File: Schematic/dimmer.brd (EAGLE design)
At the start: 51 x 51 mm, 18 parts, among them Q1 IRF840, T1 BC547

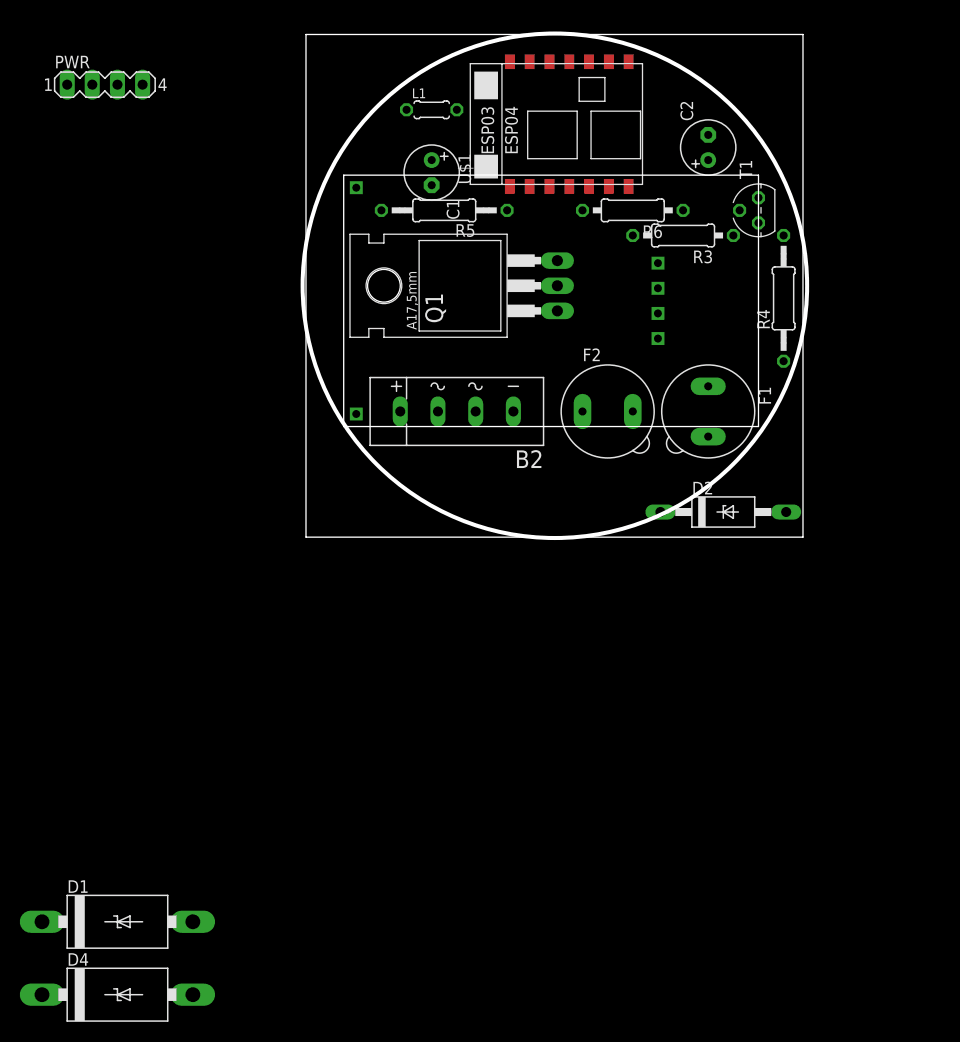
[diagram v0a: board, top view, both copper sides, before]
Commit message: Add tasters
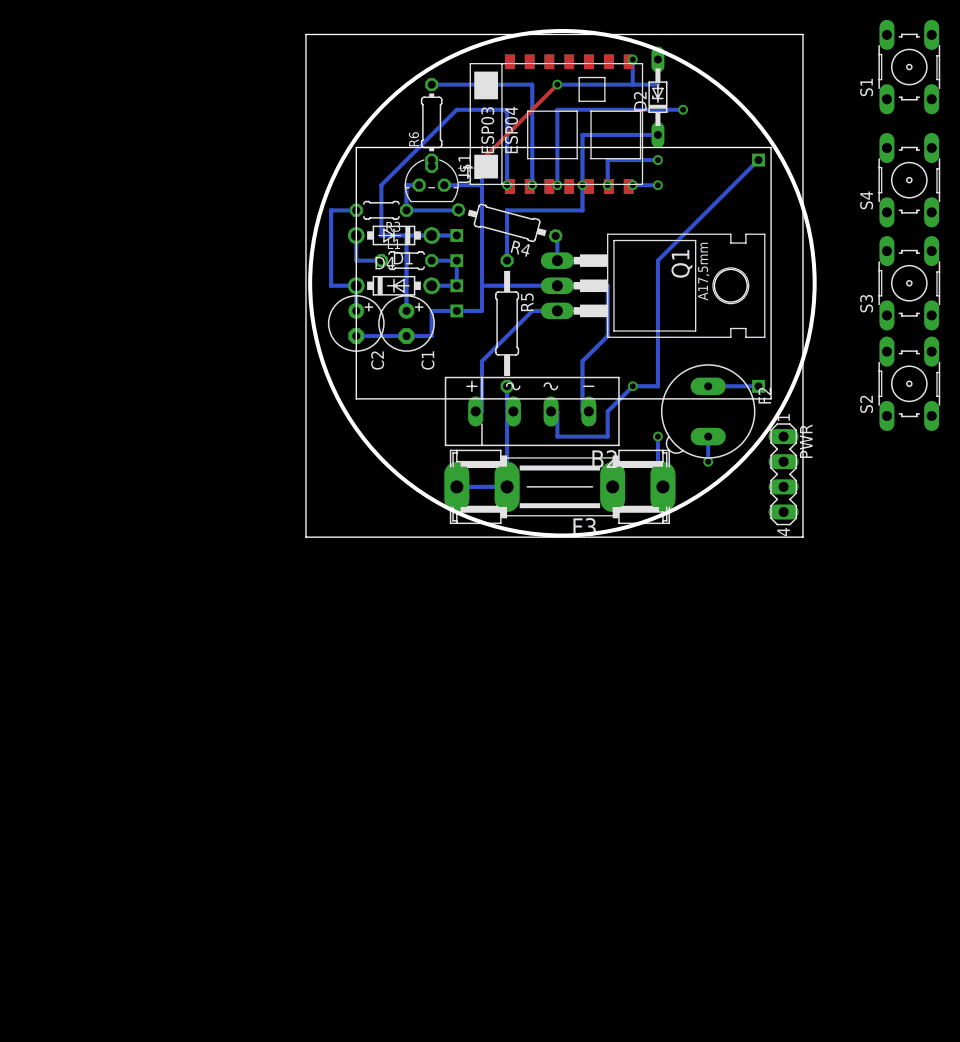
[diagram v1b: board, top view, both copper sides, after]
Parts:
- removed F1: 1A flink, fuse:19560
- added F3: 1A flink, fuse:SHK20L
- added S1, S2, S3, S4: (no value), switch-omron:B3F-10XX
- D1, D4: value 1N5819 -> 1N5817-B; device diode:C4111-15 -> diode:DO41-7.6
- D2: device diode:F126Z12 -> diode:DO34Z7
- R3: device rcl:0207/10 -> rcl:0204/5
- R4: device rcl:0207/12 -> rcl:0207/10
- R6: device rcl:0207/10 -> rcl:0204/7
- moved PWR 79.1 mm to (48.3, 6.35), turned to 270 degrees
- moved D4 76.9 mm to (8.89, 25.4)
- moved D1 74.8 mm to (8.89, 30.5), turned to 180 degrees
- moved U$2 45.8 mm to (48.3, 12.7), flipped to the top
- moved D2 42.4 mm to (35.6, 44.5), turned to 90 degrees
- moved C2 39.8 mm to (5.08, 21.6), turned to 270 degrees
- moved T1 33.1 mm to (12.7, 35.6), turned to 0 degrees
- moved R3 30.6 mm to (7.62, 33.0)
- moved R4 29.0 mm to (20.3, 31.8), turned to 165 degrees
- moved R6 22.2 mm to (12.7, 41.9), turned to 90 degrees
- moved C1 15.5 mm to (10.2, 21.6)
- moved L1 15.5 mm to (10.2, 27.9)
- moved R5 13.1 mm to (20.3, 21.6), turned to 270 degrees
- moved Q1 12.7 mm to (31.8, 25.4), turned to 270 degrees
- moved F2 10.2 mm to (40.6, 12.7), turned to 270 degrees
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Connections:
- new net N$13: S2.1, S2.2, U$1.GPIO0
- new net N$14: S3.1, S3.2, U$1.GPIO2
- new net N$15: S1.1, S1.2, U$1.GPIO18
- new net N$16: S4.1, S4.2, U$1.GPIO12
- net GND: now also S1.3, S1.4, S2.3, S2.4, S3.3, S3.4, S4.3, S4.4
- net N$17: now also B2.AC2, F3.2A; no longer B2.AC1, F1.2
- net N$31: now also F3.1A; no longer F1.1
- net N$4: now also B2.AC1; no longer B2.AC2
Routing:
- net GND: track 0.00 -> 88.0 mm, vias 0 -> 3
- net +3V3: track 0.00 -> 44.3 mm, vias 0 -> 1
- net N$4: track 0.00 -> 44.2 mm, vias 0 -> 1
- net N$7: track 0.00 -> 28.7 mm, vias 0 -> 1
- net N$16: track 0.00 -> 21.4 mm, vias 0 -> 2
- net N$12: track 0.00 -> 20.7 mm, vias 0 -> 1
- net N$17: track 0.00 -> 15.9 mm
- net N$21: track 0.00 -> 15.4 mm
- net +5V: track 0.00 -> 15.2 mm
- net N$2: track 0.00 -> 9.07 mm
- net N$14: track 0.00 -> 8.04 mm, vias 0 -> 2
- net N$6: track 0.00 -> 7.62 mm
- net N$31: track 0.00 -> 5.84 mm, vias 0 -> 1
- net N$3: track 0.00 -> 5.08 mm
- net N$9: track 0.00 -> 5.08 mm
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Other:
- board size 51 x 51 mm -> 51.4 x 51.1 mm
